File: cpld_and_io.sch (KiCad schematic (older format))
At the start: 3 parts, among them U11 5M1270ZT144C5N, U13 IS61LV5128AL-10TLI

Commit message: started routing
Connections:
- net CLK2_F is gone; now on net ~RESET_F: U11.111 (IO_2_111)
- net OE_C: now also U11.108 (IO_3_108); no longer U11.105 (IO_3_105/DIFFIO_R2P)
- net ~PAGE_F: now also U11.105 (IO_3_105/DIFFIO_R2P); no longer U11.109 (IO_2_109/DIFFIO_T9N)
- net ~RESET_F: no longer U11.108 (IO_3_108)
- net CLK_F: no longer names the net of U11.110 (IO_2_110/DIFFIO_T9P)
- no-connect marks 10 -> 12
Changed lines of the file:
@@
 Text GLabel 4420 4390 0    50   Input ~ 0
 ~BUSACK_F
-Text GLabel 4420 3990 0    50   Input ~ 0
+Text GLabel 4390 3050 0    50   Input ~ 0
 ~PAGE_F
 Text GLabel 4390 3150 0    50   Input ~ 0
 ~M1_F
-Text GLabel 4420 4090 0    50   Input ~ 0
-CLK_F
-Text GLabel 4390 3350 0    50   Output ~ 0
+Text GLabel 4420 4190 0    50   Output ~ 0
 ~RESET_F
 Text GLabel 4420 4290 0    50   Output ~ 0
@@
 Text GLabel 4390 3250 0    50   Input ~ 0
 ~RFSH~_F
-Text GLabel 4420 4190 0    50   Input ~ 0
-CLK2_F
 Text GLabel 4420 4490 0    50   Input ~ 0
 ~MREQ_F
@@
 Text GLabel 7020 1090 0    50   Input ~ 0
 RXA_F
-Text GLabel 7020 990  0    50   Output ~ 0
-TXA_F
-Text GLabel 7020 890  0    50   Input ~ 0
-RXB_F
 Text GLabel 7020 790  0    50   Output ~ 0
 TXB_F
@@
 Text GLabel 4390 2950 0    50   Output ~ 0
 OE_A
-Text GLabel 4390 3050 0    50   Output ~ 0
+Text GLabel 4390 3350 0    50   Output ~ 0
 OE_C
 Text GLabel 7040 4620 0    50   Output ~ 0
@@
 Text GLabel 7040 3330 0    50   BiDi ~ 0
 SCL
+Text GLabel 7020 890  0    50   Input ~ 0
+RXB_F
+Text GLabel 7020 990  0    50   Output ~ 0
+TXA_F
+NoConn ~ 4420 3990
+NoConn ~ 4420 4090
 $EndSCHEMATC

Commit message: mirror flipped the chips
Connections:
- net +3V3 renamed 3V3
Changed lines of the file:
@@
-$EndComp
-$Comp
-L power:+3V3 #PWR?
-U 1 1 5D01DD05
-P 2430 860
-AR Path="/5D01DD05" Ref="#PWR?"  Part="1"
-AR Path="/5CFABACD/5D01DD05" Ref="#PWR057"  Part="1"
-F 0 "#PWR057" H 2430 710 50  0001 C CNN
-F 1 "+3V3" H 2310 1020 50  0000 L CNN
-F 2 "" H 2430 860 50  0001 C CNN
-F 3 "" H 2430 860 50  0001 C CNN
-	1    2430 860
-	1    0    0    -1
 $EndComp
 $Comp
@@
 F 11 "https://www.mouser.com/ProductDetail/989-5M1270ZT144C5N" H 8648 1888 50  0001 C CNN "SPURL"
 	4    7880 3230
-	1    0    0    -1
-$EndComp
-$Comp
-L power:+3V3 #PWR?
-U 1 1 5D3E9CD7
-P 1260 2490
-AR Path="/5D3E9CD7" Ref="#PWR?"  Part="1"
-AR Path="/5D0F9837/5D3E9CD7" Ref="#PWR?"  Part="1"
-AR Path="/5CFABACD/5D3E9CD7" Ref="#PWR058"  Part="1"
-F 0 "#PWR058" H 1260 2340 50  0001 C CNN
-F 1 "+3V3" V 1275 2618 50  0000 L CNN
-F 2 "" H 1260 2490 50  0001 C CNN
-F 3 "" H 1260 2490 50  0001 C CNN
-	1    1260 2490
 	1    0    0    -1
 $EndComp
@@
 OE_G
 Wire Wire Line
-	2430 950  2430 860
-Wire Wire Line
 	2430 3550 2430 3630
 Wire Wire Line
@@
 NoConn ~ 4420 3990
 NoConn ~ 4420 4090
+Text GLabel 2430 950  1    50   Output ~ 0
+3V3
+Text GLabel 1260 2490 1    50   Output ~ 0
+3V3
 $EndSCHEMATC

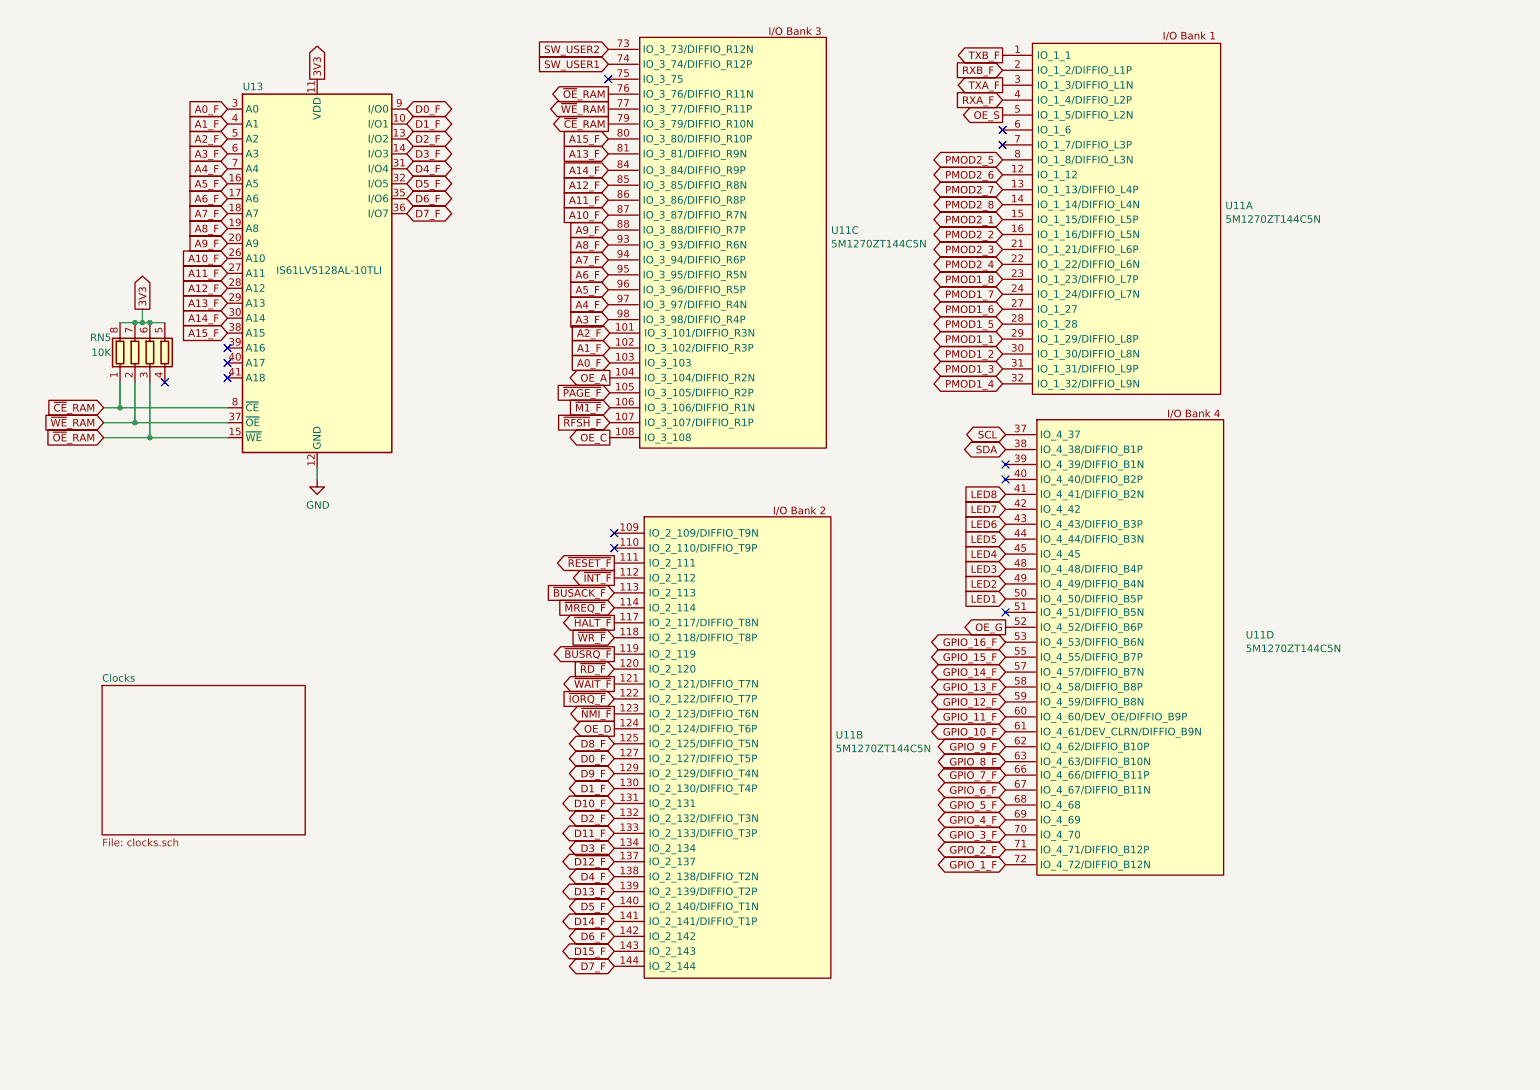
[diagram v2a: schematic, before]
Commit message: moved things around to improve routing, fixed power plane
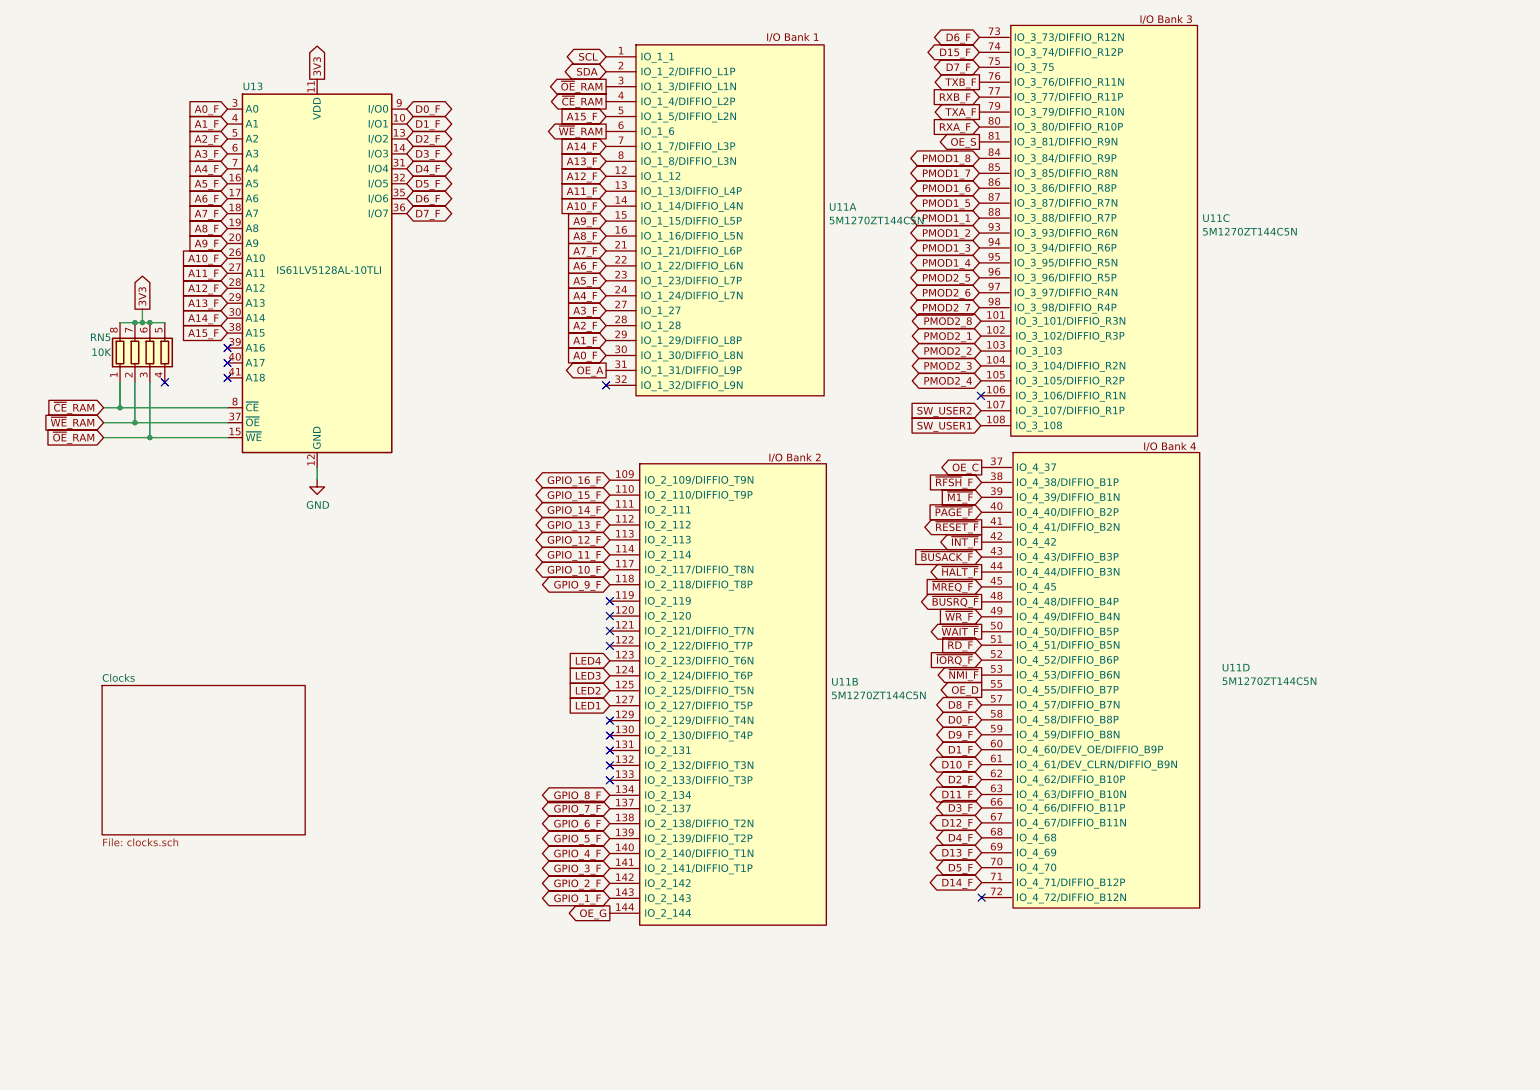
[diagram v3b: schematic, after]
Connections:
- net LED5 is gone; now on net ~HALT_F: U11.44 (IO_4_44/DIFFIO_B3N)
- net LED6 is gone; now on net ~BUSACK_F: U11.43 (IO_4_43/DIFFIO_B3P)
- net LED7 is gone; now on net ~INT_F: U11.42 (IO_4_42)
- net LED8 is gone; now on net ~RESET_F: U11.41 (IO_4_41/DIFFIO_B2N)
- net A0_F: now also U11.30 (IO_1_30/DIFFIO_L8N); no longer U11.103 (IO_3_103)
- net A10_F: now also U11.14 (IO_1_14/DIFFIO_L4N); no longer U11.87 (IO_3_87/DIFFIO_R7N)
- net A11_F: now also U11.13 (IO_1_13/DIFFIO_L4P); no longer U11.86 (IO_3_86/DIFFIO_R8P)
- net A12_F: now also U11.12 (IO_1_12); no longer U11.85 (IO_3_85/DIFFIO_R8N)
- net A13_F: now also U11.8 (IO_1_8/DIFFIO_L3N); no longer U11.81 (IO_3_81/DIFFIO_R9N)
- net A14_F: now also U11.7 (IO_1_7/DIFFIO_L3P); no longer U11.84 (IO_3_84/DIFFIO_R9P)
- net A15_F: now also U11.5 (IO_1_5/DIFFIO_L2N); no longer U11.80 (IO_3_80/DIFFIO_R10P)
- net A1_F: now also U11.29 (IO_1_29/DIFFIO_L8P); no longer U11.102 (IO_3_102/DIFFIO_R3P)
- net A2_F: now also U11.28 (IO_1_28); no longer U11.101 (IO_3_101/DIFFIO_R3N)
- net A3_F: now also U11.27 (IO_1_27); no longer U11.98 (IO_3_98/DIFFIO_R4P)
- net A4_F: now also U11.24 (IO_1_24/DIFFIO_L7N); no longer U11.97 (IO_3_97/DIFFIO_R4N)
- net A5_F: now also U11.23 (IO_1_23/DIFFIO_L7P); no longer U11.96 (IO_3_96/DIFFIO_R5P)
- net A6_F: now also U11.22 (IO_1_22/DIFFIO_L6N); no longer U11.95 (IO_3_95/DIFFIO_R5N)
- net A7_F: now also U11.21 (IO_1_21/DIFFIO_L6P); no longer U11.94 (IO_3_94/DIFFIO_R6P)
- net A8_F: now also U11.16 (IO_1_16/DIFFIO_L5N); no longer U11.93 (IO_3_93/DIFFIO_R6N)
- net A9_F: now also U11.15 (IO_1_15/DIFFIO_L5P); no longer U11.88 (IO_3_88/DIFFIO_R7P)
- net D0_F: now also U11.58 (IO_4_58/DIFFIO_B8P); no longer U11.127 (IO_2_127/DIFFIO_T5P)
- net D10_F: now also U11.61 (IO_4_61/DEV_CLRN/DIFFIO_B9N); no longer U11.131 (IO_2_131)
- net D11_F: now also U11.63 (IO_4_63/DIFFIO_B10N); no longer U11.133 (IO_2_133/DIFFIO_T3P)
- net D12_F: now also U11.67 (IO_4_67/DIFFIO_B11N); no longer U11.137 (IO_2_137)
- net D13_F: now also U11.69 (IO_4_69); no longer U11.139 (IO_2_139/DIFFIO_T2P)
- net D14_F: now also U11.71 (IO_4_71/DIFFIO_B12P); no longer U11.141 (IO_2_141/DIFFIO_T1P)
- net D15_F: now also U11.74 (IO_3_74/DIFFIO_R12P); no longer U11.143 (IO_2_143)
- net D1_F: now also U11.60 (IO_4_60/DEV_OE/DIFFIO_B9P); no longer U11.130 (IO_2_130/DIFFIO_T4P)
- net D2_F: now also U11.62 (IO_4_62/DIFFIO_B10P); no longer U11.132 (IO_2_132/DIFFIO_T3N)
- net D3_F: now also U11.66 (IO_4_66/DIFFIO_B11P); no longer U11.134 (IO_2_134)
- net D4_F: now also U11.68 (IO_4_68); no longer U11.138 (IO_2_138/DIFFIO_T2N)
- net D5_F: now also U11.70 (IO_4_70); no longer U11.140 (IO_2_140/DIFFIO_T1N)
- net D6_F: now also U11.73 (IO_3_73/DIFFIO_R12N); no longer U11.142 (IO_2_142)
- net D7_F: now also U11.75 (IO_3_75); no longer U11.144 (IO_2_144)
- net D8_F: now also U11.57 (IO_4_57/DIFFIO_B7N); no longer U11.125 (IO_2_125/DIFFIO_T5N)
- net D9_F: now also U11.59 (IO_4_59/DIFFIO_B8N); no longer U11.129 (IO_2_129/DIFFIO_T4N)
- net GPIO_10_F: now also U11.117 (IO_2_117/DIFFIO_T8N); no longer U11.61 (IO_4_61/DEV_CLRN/DIFFIO_B9N)
- net GPIO_11_F: now also U11.114 (IO_2_114); no longer U11.60 (IO_4_60/DEV_OE/DIFFIO_B9P)
- net GPIO_12_F: now also U11.113 (IO_2_113); no longer U11.59 (IO_4_59/DIFFIO_B8N)
- net GPIO_13_F: now also U11.112 (IO_2_112); no longer U11.58 (IO_4_58/DIFFIO_B8P)
- net GPIO_14_F: now also U11.111 (IO_2_111); no longer U11.57 (IO_4_57/DIFFIO_B7N)
- net GPIO_15_F: now also U11.110 (IO_2_110/DIFFIO_T9P); no longer U11.55 (IO_4_55/DIFFIO_B7P)
- net GPIO_16_F: now also U11.109 (IO_2_109/DIFFIO_T9N); no longer U11.53 (IO_4_53/DIFFIO_B6N)
- net GPIO_1_F: now also U11.143 (IO_2_143); no longer U11.72 (IO_4_72/DIFFIO_B12N)
- net GPIO_2_F: now also U11.142 (IO_2_142); no longer U11.71 (IO_4_71/DIFFIO_B12P)
- net GPIO_3_F: now also U11.141 (IO_2_141/DIFFIO_T1P); no longer U11.70 (IO_4_70)
- net GPIO_4_F: now also U11.140 (IO_2_140/DIFFIO_T1N); no longer U11.69 (IO_4_69)
- net GPIO_5_F: now also U11.139 (IO_2_139/DIFFIO_T2P); no longer U11.68 (IO_4_68)
- net GPIO_6_F: now also U11.138 (IO_2_138/DIFFIO_T2N); no longer U11.67 (IO_4_67/DIFFIO_B11N)
- net GPIO_7_F: now also U11.137 (IO_2_137); no longer U11.66 (IO_4_66/DIFFIO_B11P)
- net GPIO_8_F: now also U11.134 (IO_2_134); no longer U11.63 (IO_4_63/DIFFIO_B10N)
- net GPIO_9_F: now also U11.118 (IO_2_118/DIFFIO_T8P); no longer U11.62 (IO_4_62/DIFFIO_B10P)
- net LED1: now also U11.127 (IO_2_127/DIFFIO_T5P); no longer U11.50 (IO_4_50/DIFFIO_B5P)
- net LED2: now also U11.125 (IO_2_125/DIFFIO_T5N); no longer U11.49 (IO_4_49/DIFFIO_B4N)
- net LED3: now also U11.124 (IO_2_124/DIFFIO_T6P); no longer U11.48 (IO_4_48/DIFFIO_B4P)
- net LED4: now also U11.123 (IO_2_123/DIFFIO_T6N); no longer U11.45 (IO_4_45)
- net OE_A: now also U11.31 (IO_1_31/DIFFIO_L9P); no longer U11.104 (IO_3_104/DIFFIO_R2N)
- net OE_C: now also U11.37 (IO_4_37); no longer U11.108 (IO_3_108)
- net OE_D: now also U11.55 (IO_4_55/DIFFIO_B7P); no longer U11.124 (IO_2_124/DIFFIO_T6P)
- net OE_G: now also U11.144 (IO_2_144); no longer U11.52 (IO_4_52/DIFFIO_B6P)
- net OE_S: now also U11.81 (IO_3_81/DIFFIO_R9N); no longer U11.5 (IO_1_5/DIFFIO_L2N)
- net PMOD1_1: now also U11.88 (IO_3_88/DIFFIO_R7P); no longer U11.29 (IO_1_29/DIFFIO_L8P)
- net PMOD1_2: now also U11.93 (IO_3_93/DIFFIO_R6N); no longer U11.30 (IO_1_30/DIFFIO_L8N)
- net PMOD1_3: now also U11.94 (IO_3_94/DIFFIO_R6P); no longer U11.31 (IO_1_31/DIFFIO_L9P)
- net PMOD1_4: now also U11.95 (IO_3_95/DIFFIO_R5N); no longer U11.32 (IO_1_32/DIFFIO_L9N)
- net PMOD1_5: now also U11.87 (IO_3_87/DIFFIO_R7N); no longer U11.28 (IO_1_28)
- net PMOD1_6: now also U11.86 (IO_3_86/DIFFIO_R8P); no longer U11.27 (IO_1_27)
- net PMOD1_7: now also U11.85 (IO_3_85/DIFFIO_R8N); no longer U11.24 (IO_1_24/DIFFIO_L7N)
- net PMOD1_8: now also U11.84 (IO_3_84/DIFFIO_R9P); no longer U11.23 (IO_1_23/DIFFIO_L7P)
- net PMOD2_1: now also U11.102 (IO_3_102/DIFFIO_R3P); no longer U11.15 (IO_1_15/DIFFIO_L5P)
- net PMOD2_2: now also U11.103 (IO_3_103); no longer U11.16 (IO_1_16/DIFFIO_L5N)
- net PMOD2_3: now also U11.104 (IO_3_104/DIFFIO_R2N); no longer U11.21 (IO_1_21/DIFFIO_L6P)
- net PMOD2_4: now also U11.105 (IO_3_105/DIFFIO_R2P); no longer U11.22 (IO_1_22/DIFFIO_L6N)
- net PMOD2_5: now also U11.96 (IO_3_96/DIFFIO_R5P); no longer U11.8 (IO_1_8/DIFFIO_L3N)
- net PMOD2_6: now also U11.97 (IO_3_97/DIFFIO_R4N); no longer U11.12 (IO_1_12)
- net PMOD2_7: now also U11.98 (IO_3_98/DIFFIO_R4P); no longer U11.13 (IO_1_13/DIFFIO_L4P)
- net PMOD2_8: now also U11.101 (IO_3_101/DIFFIO_R3N); no longer U11.14 (IO_1_14/DIFFIO_L4N)
- net RXA_F: now also U11.80 (IO_3_80/DIFFIO_R10P); no longer U11.4 (IO_1_4/DIFFIO_L2P)
- net RXB_F: now also U11.77 (IO_3_77/DIFFIO_R11P); no longer U11.2 (IO_1_2/DIFFIO_L1P)
- net SCL: now also U11.1 (IO_1_1); no longer U11.37 (IO_4_37)
- net SDA: now also U11.2 (IO_1_2/DIFFIO_L1P); no longer U11.38 (IO_4_38/DIFFIO_B1P)
- net SW_USER1: now also U11.108 (IO_3_108); no longer U11.74 (IO_3_74/DIFFIO_R12P)
- net SW_USER2: now also U11.107 (IO_3_107/DIFFIO_R1P); no longer U11.73 (IO_3_73/DIFFIO_R12N)
- net TXA_F: now also U11.79 (IO_3_79/DIFFIO_R10N); no longer U11.3 (IO_1_3/DIFFIO_L1N)
- net TXB_F: now also U11.76 (IO_3_76/DIFFIO_R11N); no longer U11.1 (IO_1_1)
- net ~BUSACK_F: no longer U11.113 (IO_2_113)
- net ~BUSRQ_F: now also U11.48 (IO_4_48/DIFFIO_B4P); no longer U11.119 (IO_2_119)
- net ~CE~_RAM: now also U11.4 (IO_1_4/DIFFIO_L2P); no longer U11.79 (IO_3_79/DIFFIO_R10N)
- net ~HALT_F: no longer U11.117 (IO_2_117/DIFFIO_T8N)
- net ~INT_F: no longer U11.112 (IO_2_112)
- net ~IORQ_F: now also U11.52 (IO_4_52/DIFFIO_B6P); no longer U11.122 (IO_2_122/DIFFIO_T7P)
- net ~M1_F: now also U11.39 (IO_4_39/DIFFIO_B1N); no longer U11.106 (IO_3_106/DIFFIO_R1N)
- net ~MREQ_F: now also U11.45 (IO_4_45); no longer U11.114 (IO_2_114)
- net ~NMI_F: now also U11.53 (IO_4_53/DIFFIO_B6N); no longer U11.123 (IO_2_123/DIFFIO_T6N)
- net ~OE~_RAM: now also U11.3 (IO_1_3/DIFFIO_L1N); no longer U11.76 (IO_3_76/DIFFIO_R11N)
- net ~PAGE_F: now also U11.40 (IO_4_40/DIFFIO_B2P); no longer U11.105 (IO_3_105/DIFFIO_R2P)
- net ~RD_F: now also U11.51 (IO_4_51/DIFFIO_B5N); no longer U11.120 (IO_2_120)
- net ~RESET_F: no longer U11.111 (IO_2_111)
- net ~RFSH~_F: now also U11.38 (IO_4_38/DIFFIO_B1P); no longer U11.107 (IO_3_107/DIFFIO_R1P)
- net ~WAIT_F: now also U11.50 (IO_4_50/DIFFIO_B5P); no longer U11.121 (IO_2_121/DIFFIO_T7N)
- net ~WE~_RAM: now also U11.6 (IO_1_6); no longer U11.77 (IO_3_77/DIFFIO_R11P)
- net ~WR_F: now also U11.49 (IO_4_49/DIFFIO_B4N); no longer U11.118 (IO_2_118/DIFFIO_T8P)
- no-connect marks 12 -> 16
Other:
- moved on the sheet: U11A, U11B, U11C, U11D

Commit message: replaced some global pins with hierarchical sheet pins
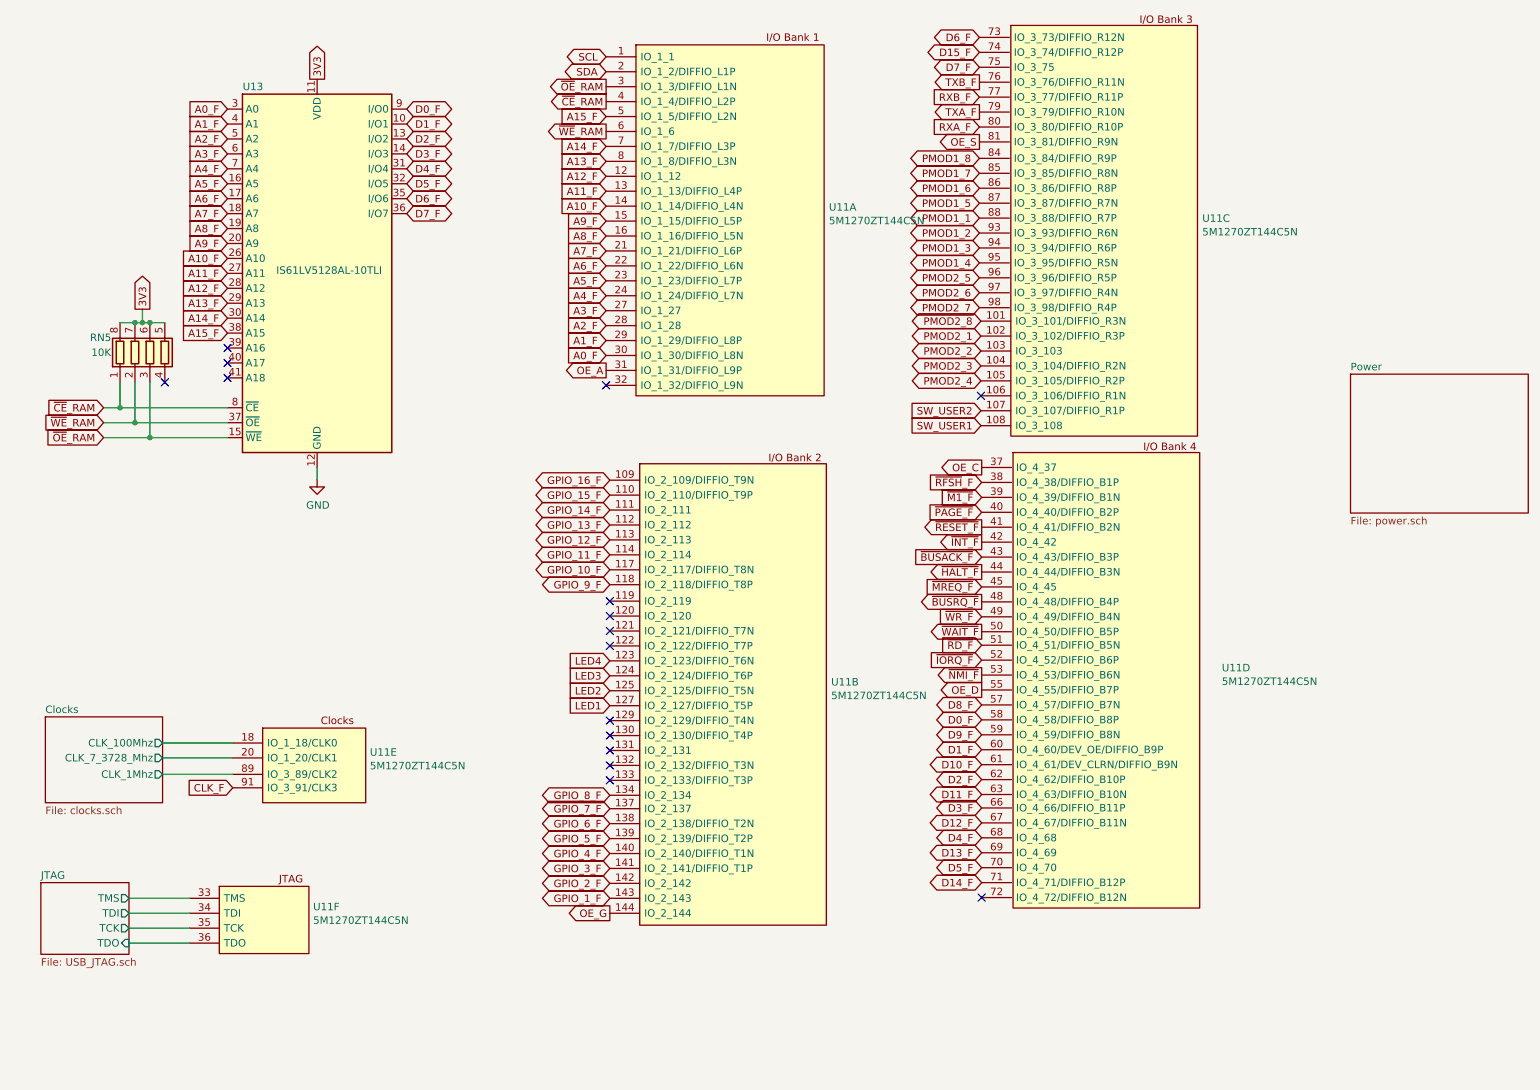
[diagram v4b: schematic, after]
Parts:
- added unit 6 of U11
- added unit 5 of U11
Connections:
- new net CLK_F: U11.91 (IO_3_91/CLK3)
- new net Clocks/CLK_100Mhz: U11.18 (IO_1_18/CLK0)
- new net Clocks/CLK_1Mhz: U11.89 (IO_3_89/CLK2)
- new net Clocks/CLK_7_3728_Mhz: U11.20 (IO_1_20/CLK1)
- new net JTAG/TCK: U11.35 (TCK)
- new net JTAG/TDI: U11.34 (TDI)
- new net JTAG/TDO: U11.36 (TDO)
- new net JTAG/TMS: U11.33 (TMS)
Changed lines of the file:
@@
 $Descr A4 11693 8268
 encoding utf-8
-Sheet 3 6
+Sheet 2 6
 Title ""
 Date ""
@@
 $EndDescr
 $Sheet
-S 990  5010 1360 1000
+S 610  5220 785  575
 U 5CFFC458
 F0 "Clocks" 50
 F1 "clocks.sch" 50
+F2 "CLK_100Mhz" O R 1395 5395 50
+F3 "CLK_7_3728_Mhz" O R 1395 5495 50
+F4 "CLK_1Mhz" O R 1395 5605 50
 $EndSheet
 $Comp
@@
 NoConn ~ 4390 5645
 NoConn ~ 4390 5245
+$Sheet
+S 580  6330 590  480
+U 5D0BF766
+F0 "JTAG" 50
+F1 "USB_JTAG.sch" 50
+F2 "TCK" O R 1170 6635 50
+F3 "TDI" O R 1170 6535 50
+F4 "TDO" I R 1170 6735 50
+F5 "TMS" O R 1170 6435 50
+$EndSheet
+$Comp
+L rc2014_max_v-rescue:5M1270ZT144C5N-CPLD_Altera U?
+U 6 1 5D1673E5
+P 2085 6355
+AR Path="/5D1673E5" Ref="U?"  Part="6"
+AR Path="/5D0F9837/5D1673E5" Ref="U?"  Part="6"
+AR Path="/5CFABACD/5D0BF766/5D1673E5" Ref="U?"  Part="6"
+AR Path="/5CFABACD/5D1673E5" Ref="U11"  Part="6"
+F 0 "U11" H 2403 6218 50  0000 L CNN
+F 1 "5M1270ZT144C5N" H 2403 6127 50  0000 L CNN
+F 2 "Package_QFP:TQFP-144_20x20mm_P0.5mm" H 3925 9255 50  0001 L CNN
+F 3 "https://www.mouser.com/datasheet/2/612/max5_handbook-1098935.pdf" H 3925 9155 50  0001 L CNN
+F 4 "CPLD - Complex Programmable Logic Devices CPLD - MAX V 980 Macro 114 IOs" H 3925 9055 50  0001 L CNN "Description"
+F 5 "1.55" H 3925 8955 50  0001 L CNN "Height"
+F 6 "Intel" H 2085 6355 50  0001 C CNN "MFR"
+F 7 "5M1270ZT144C5N" H 2085 6355 50  0001 C CNN "MPN"
+F 8 "5M1270ZT144C5N" H 3925 8555 50  0001 L CNN "Manufacturer_Part_Number"
+F 9 "989-5M1270ZT144C5N" H 2403 6318 50  0001 C CNN "SPN"
+F 10 "Mouser" H 2085 6355 50  0001 C CNN "SPR"
+F 11 "https://www.mouser.com/ProductDetail/989-5M1270ZT144C5N" H 2403 6318 50  0001 C CNN "SPURL"
+	6    2085 6355
+	1    0    0    -1
+$EndComp
+$Comp
+L rc2014_max_v-rescue:5M1270ZT144C5N-CPLD_Altera U?
+U 5 1 5D1C4FEB
+P 2425 5295
+AR Path="/5D0F9837/5D1C4FEB" Ref="U?"  Part="5"
+AR Path="/5CFABACD/5D1C4FEB" Ref="U11"  Part="5"
+AR Path="/5CFABACD/5CFFC458/5D1C4FEB" Ref="U?"  Part="5"
+AR Path="/5D1C4FEB" Ref="U?"  Part="5"
+F 0 "U11" H 2783 5133 50  0000 L CNN
+F 1 "5M1270ZT144C5N" H 2783 5042 50  0000 L CNN
+F 2 "Package_QFP:TQFP-144_20x20mm_P0.5mm" H 4265 8195 50  0001 L CNN
+F 3 "https://www.mouser.com/datasheet/2/612/max5_handbook-1098935.pdf" H 4265 8095 50  0001 L CNN
+F 4 "CPLD - Complex Programmable Logic Devices CPLD - MAX V 980 Macro 114 IOs" H 4265 7995 50  0001 L CNN "Description"
+F 5 "1.55" H 4265 7895 50  0001 L CNN "Height"
+F 6 "Intel" H 2425 5295 50  0001 C CNN "MFR"
+F 7 "5M1270ZT144C5N" H 2425 5295 50  0001 C CNN "MPN"
+F 8 "5M1270ZT144C5N" H 4265 7495 50  0001 L CNN "Manufacturer_Part_Number"
+F 9 "989-5M1270ZT144C5N" H 2783 5233 50  0001 C CNN "SPN"
+F 10 "Mouser" H 2425 5295 50  0001 C CNN "SPR"
+F 11 "https://www.mouser.com/ProductDetail/989-5M1270ZT144C5N" H 2783 5233 50  0001 C CNN "SPURL"
+	5    2425 5295
+	1    0    0    -1
+$EndComp
+Text GLabel 1865 5695 0    50   Input ~ 0
+CLK_F
+$Sheet
+S 9350 2925 1190 930
+U 5D2103A8
+F0 "Power" 50
+F1 "power.sch" 50
+$EndSheet
+Wire Wire Line
+	1395 5605 1865 5605
+Wire Wire Line
+	1395 5495 1865 5495
+Wire Wire Line
+	1395 5395 1865 5395
+Wire Wire Line
+	1170 6435 1575 6435
+Wire Wire Line
+	1170 6535 1575 6535
+Wire Wire Line
+	1170 6635 1575 6635
+Wire Wire Line
+	1170 6735 1575 6735
 $EndSCHEMATC
